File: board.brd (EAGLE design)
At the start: 26.3 x 37.5 mm, 49 parts, among them IC1 ATMEGA48/88/168-AU, IC2 TP4056, IC3 MAX31865, Q1 IRFR5305

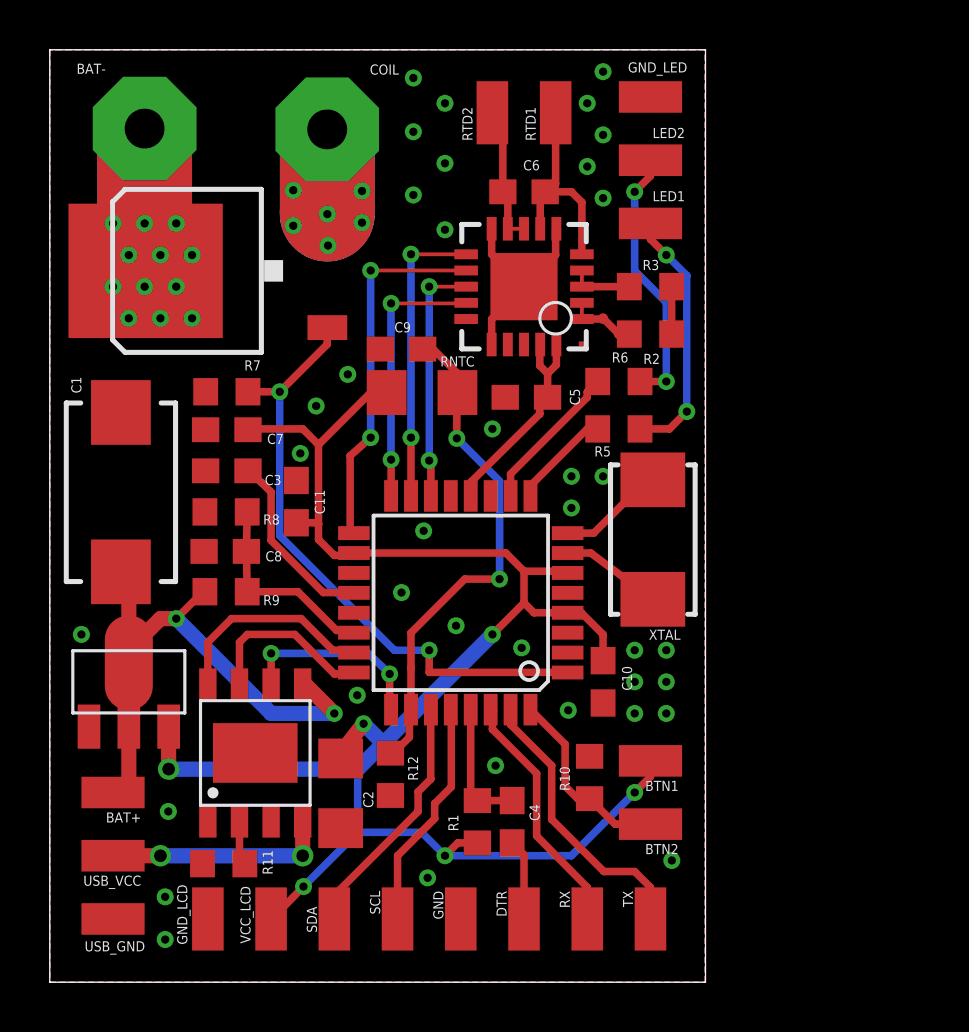
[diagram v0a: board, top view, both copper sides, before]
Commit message: cleanup of schematics
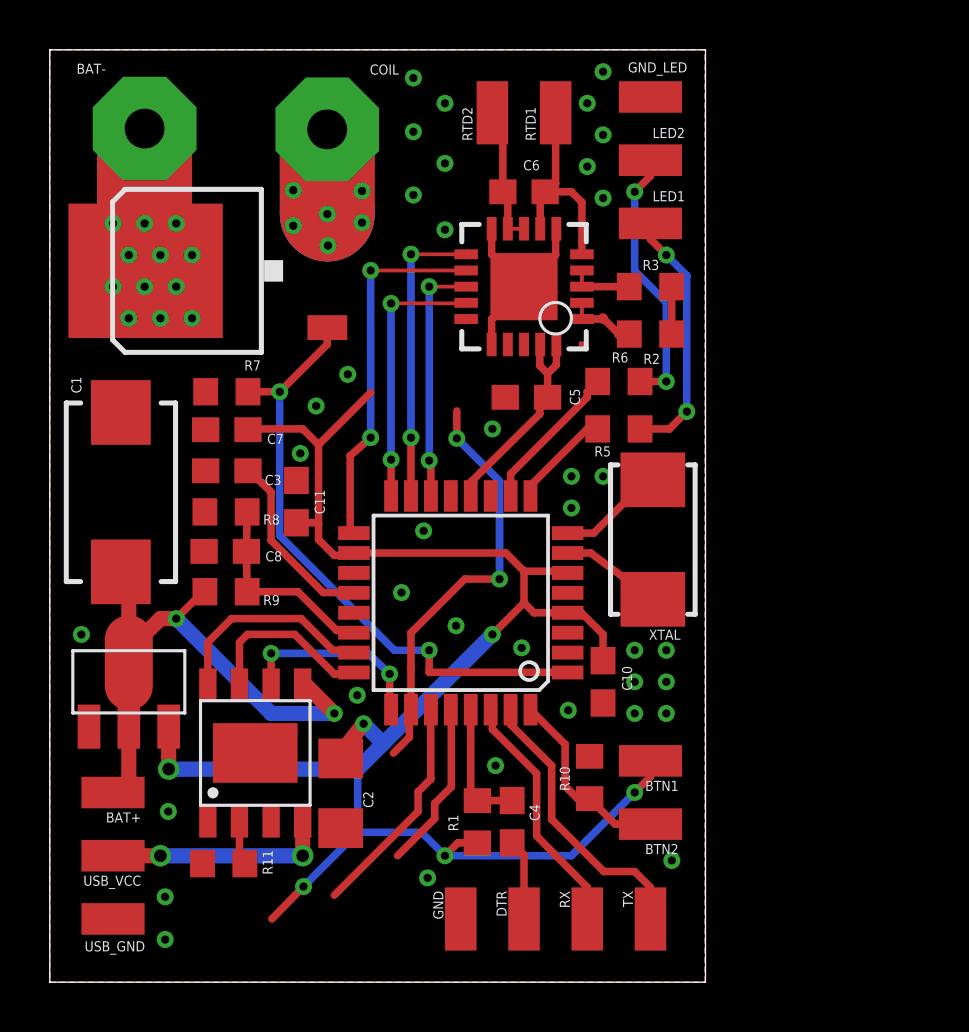
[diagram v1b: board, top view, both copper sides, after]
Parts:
- removed C9: 100n, rcl:C0603
- removed GND_LCD, SCL, SDA, VCC_LCD: (no value), wirepad:SMD1,27-2,54
- removed R12: 5.6k, rcl:R0603
- removed RNTC: (no value), resistor:R1206
- R11: value 10k -> 1,2k
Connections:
- net A3_NTC: no longer C9.2, R12.2, RNTC.2
- net A4_SDA: no longer SDA.1
- net A5_SCL: no longer SCL.1
- net GND: no longer C9.1, GND_LCD.1, R12.1
- net VCC: no longer RNTC.1, VCC_LCD.1
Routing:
- net A3_NTC: track 20.5 -> 17.0 mm
- net A5_SCL: track 9.31 -> 6.77 mm
- net A4_SDA: track 10.0 -> 9.06 mm
- net VCC: track 72.5 -> 71.9 mm

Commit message: using smaller resistors for voltage sensor
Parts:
- R8: value 10k -> 100k
- R9: value 5k -> 51k
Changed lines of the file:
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@@
 <attribute name="VALUE" x="6.477" y="21.81225" size="1.27" layer="27"/>
 </element>
-<element name="R8" library="rcl" package="R0603" value="10k" x="7.08025" y="18.89125" smashed="yes" rot="R180">
+<element name="R8" library="rcl" package="R0603" value="100k" x="7.08025" y="18.89125" smashed="yes" rot="R180">
 <attribute name="NAME" x="8.5725" y="18.38325" size="0.4064" layer="25"/>
 <attribute name="VALUE" x="7.71525" y="20.79625" size="1.27" layer="27" rot="R180"/>
 </element>
-<element name="R9" library="rcl" package="R0603" value="5k" x="7.08025" y="15.6845" smashed="yes">
+<element name="R9" library="rcl" package="R0603" value="51k" x="7.08025" y="15.6845" smashed="yes">
 <attribute name="NAME" x="8.5725" y="15.14475" size="0.4064" layer="25"/>
 <attribute name="VALUE" x="6.44525" y="13.7795" size="1.27" layer="27"/>

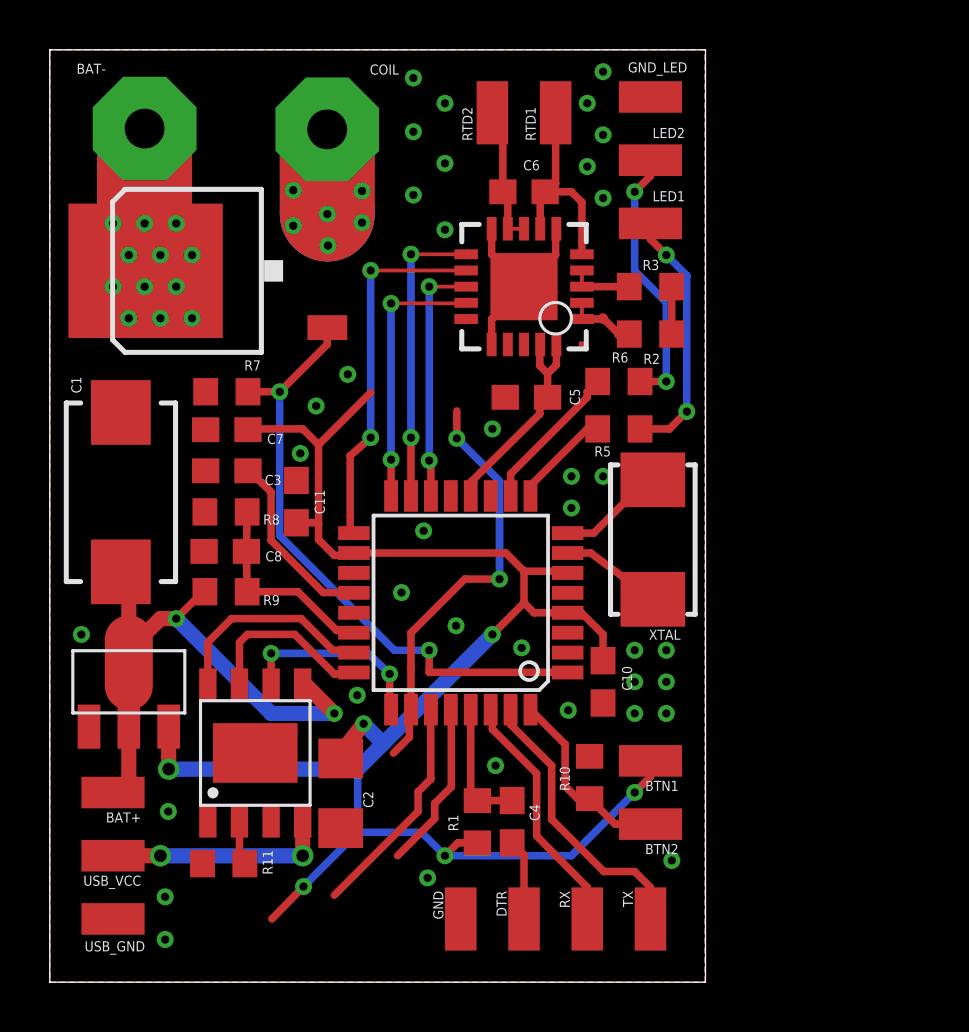
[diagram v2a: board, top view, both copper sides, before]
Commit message: using new mosfets, rearangement of parts
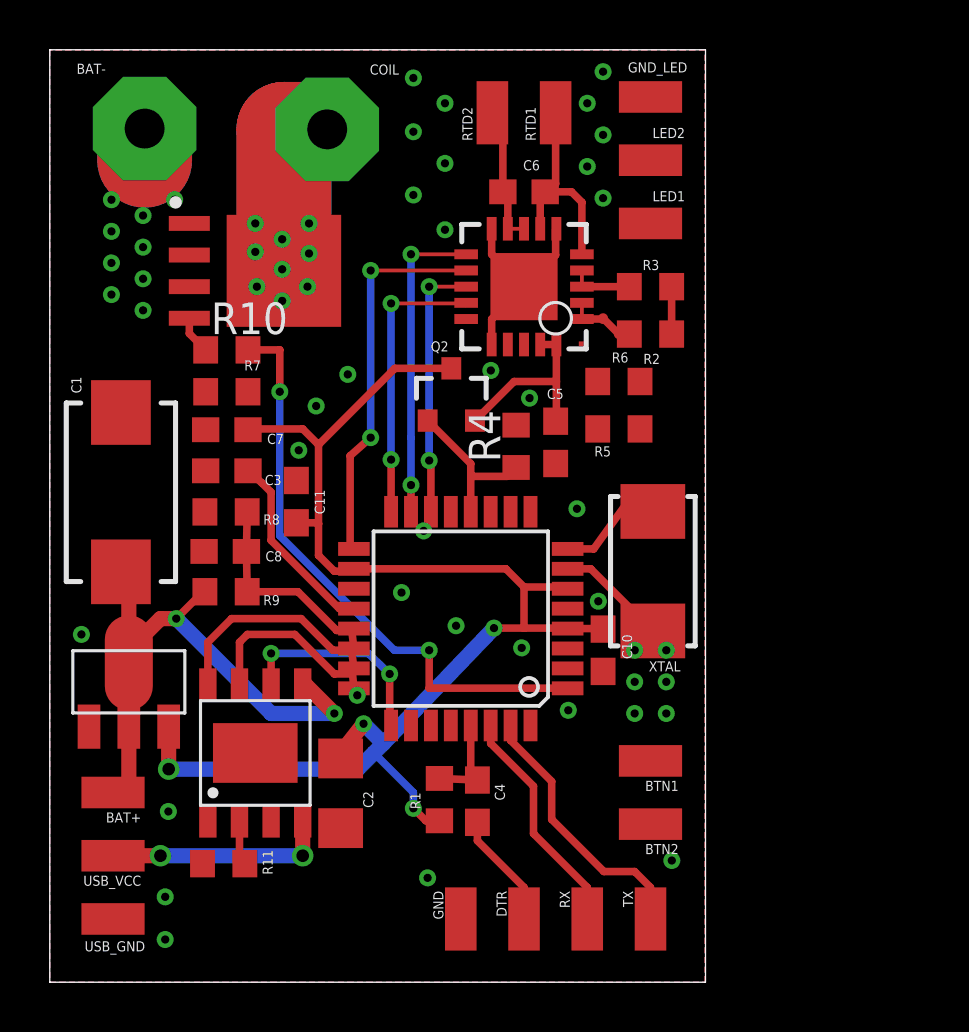
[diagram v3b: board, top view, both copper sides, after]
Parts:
- added Q2: IRLML2244, SparkFun-DiscreteSemi:SOT23-3
- added R4: 10k, rcl:R0603
- Q1: value IRFR5305 -> PH2925U; device transistor-power:D-PAK_TO252AA -> selfmade:SOT-669
- R10: value 10k -> 100
- moved R10 22.5 mm to (7.11, 25.4), turned to 0 degrees
- moved Q1 3.18 mm to (9.53, 28.6), turned to 0 degrees
- moved C5 2.16 mm to (20.3, 21.7), turned to 270 degrees
- moved R1 1.76 mm to (15.7, 7.33)
- moved C4 1.62 mm to (17.2, 7.27)
- moved C10 1.27 mm to (22.2, 13.3)
- moved XTAL 1.27 mm to (24.2, 16.5)
- moved IC1 0.63 mm to (16.5, 14.6)
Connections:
- net A3_NTC renamed A3
- net A4_SDA renamed A4
- net A5_SCL renamed A5
- new net GATE: Q1.4, R10.1, R7.2
- new net VCC_MAX: C5.1, IC3.19, IC3.20, Q2.2
- net COIL: now also Q1.5; no longer Q1.3
- net D2_BUTTON: now also BTN1.1; no longer BTN2.1, R10.1
- net D3_GATE: now also R10.2; no longer Q1.1, R7.2
- net D8_VCC_MAX: now also Q2.1, R4.1; no longer C5.1, IC3.19, IC3.20
- net GND: now also Q1.1, Q1.2, Q1.3, R4.2; no longer Q1.4, R10.2
- net VCC: now also Q2.3; no longer BTN1.1
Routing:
- net A3: track 17.0 -> 0.00 mm, vias 2 -> 0
- net VCC: track 71.9 -> 56.0 mm, vias 6 -> 4
- net LED2: track 10.7 -> 0.00 mm, vias 2 -> 0
- net LED1: track 10.3 -> 0.00 mm, vias 2 -> 0
- net A4: track 9.06 -> 0.00 mm
- net COIL: track 6.82 -> 14.8 mm, vias 6 -> 0
- net D2_BUTTON: track 7.71 -> 0.00 mm
- net VCC_MAX: track 0.00 -> 7.66 mm
- net GND: track 18.2 -> 10.6 mm, vias 49 -> 45
- net A5: track 6.77 -> 0.00 mm
- net D6_LED2: track 6.05 -> 0.00 mm
- net D5_LED1: track 4.06 -> 0.00 mm
- net D8_VCC_MAX: track 8.82 -> 6.35 mm
- net GATE: track 0.00 -> 1.54 mm
- net RST: track 5.32 -> 3.83 mm
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
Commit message: adding 3rd LED, new regulator, shrinking board
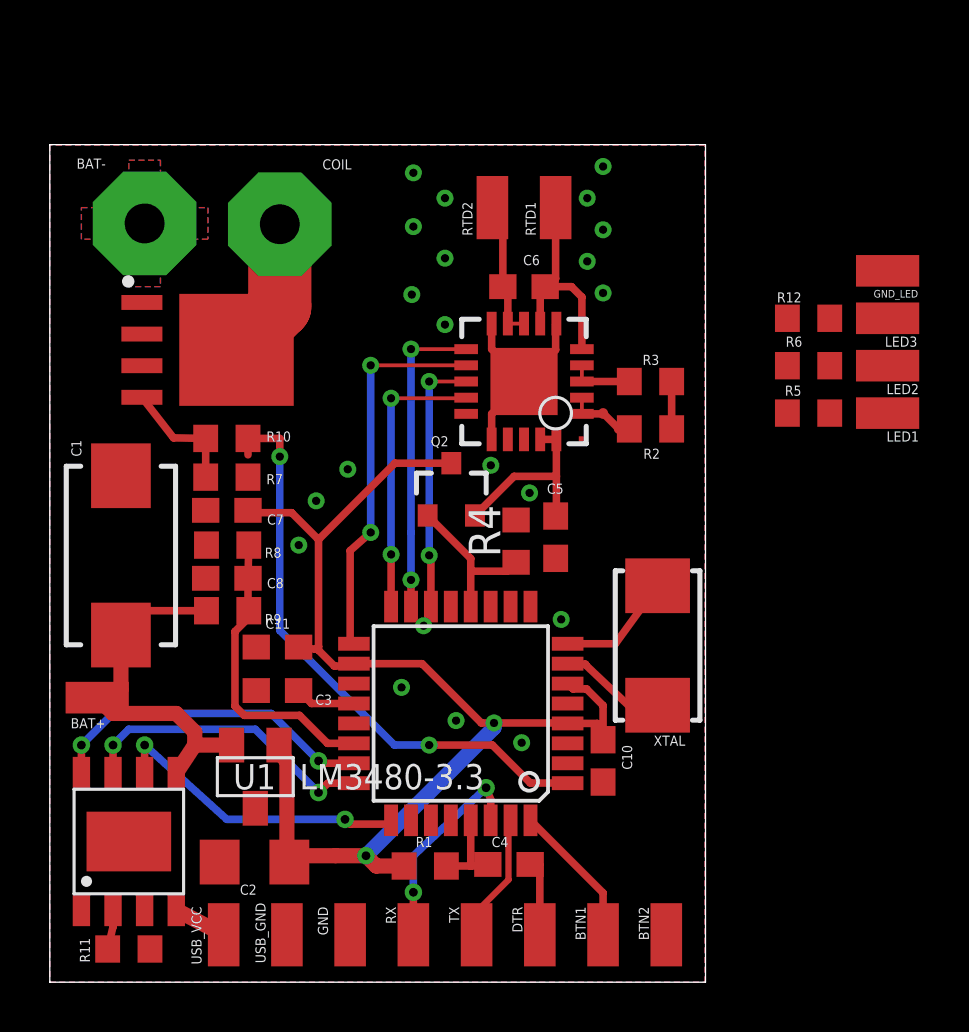
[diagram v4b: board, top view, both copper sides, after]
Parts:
- removed U$2: TS9011, selfmade:SOT89
- added LED3: (no value), wirepad:SMD1,27-2,54
- added R12: 1K, rcl:R0603
- added U1: LM3480-3.3, regulators:SOT-23-3
- moved LED2 12.6 mm to (33.7, 24.8)
- moved LED1 12.2 mm to (33.7, 22.9)
- moved GND_LED 11.8 mm to (33.7, 28.6)
- moved C3 9.06 mm to (9.14, 11.7)
- moved R5 7.65 mm to (30.5, 22.9)
- moved R6 7.65 mm to (30.5, 24.8)
- moved BTN1 7.24 mm to (22.2, 1.91), turned to 180 degrees
- moved USB_GND 7.01 mm to (9.53, 1.91), turned to 180 degrees
- moved RX 7.01 mm to (14.6, 1.91)
- moved TX 7.01 mm to (17.1, 1.91)
- moved IC2 6.20 mm to (3.17, 5.65)
- moved C11 5.89 mm to (9.14, 13.5), turned to 0 degrees
- moved USB_VCC 5.46 mm to (6.99, 1.91), turned to 180 degrees
- moved R11 5.13 mm to (3.17, 1.33), turned to 0 degrees
- moved GND 4.49 mm to (12.1, 1.91)
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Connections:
- removed net D9: IC1.13
- new net D9_LED3: IC1.13, R12.2
- new net LED3: LED3.1, R12.1
- net GND: now also BTN2.1, U1.3; no longer U$2.GND
- net VBAT: now also U1.2; no longer U$2.IN1, U$2.IN2
- net VCC: now also U1.1; no longer U$2.OUT
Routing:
- net COIL: track 14.8 -> 5.22 mm
- net VCC: track 56.0 -> 48.7 mm, vias 4 -> 2
- net VUSB: track 9.00 -> 2.15 mm, vias 2 -> 0
- net VBAT: track 20.9 -> 14.9 mm, vias 2 -> 0
- net D2_BUTTON: track 0.00 -> 5.80 mm
- net TXO: track 10.8 -> 5.16 mm
- net AREF: track 7.66 -> 2.44 mm
- net A1_CHRG_STAT: track 7.60 -> 12.3 mm, vias 0 -> 2
- net A0_CHRG_EN: track 9.12 -> 13.4 mm, vias 0 -> 2
- net A2_CHRG_STBY: track 8.42 -> 12.3 mm
- net GATE: track 1.54 -> 4.91 mm
- net A7_VSENS: track 8.78 -> 12.1 mm
- net GND: track 10.6 -> 8.06 mm, vias 45 -> 21
- net DTR: track 4.66 -> 3.21 mm
- net RXI: track 9.38 -> 8.72 mm, vias 0 -> 2
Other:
- board size 26.3 x 37.5 mm -> 26.3 x 33.6 mm
- board text added: "Vapoduino_v0.2"
- board text removed: "Vapoduino_v0.1"

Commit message: first draft of new layout
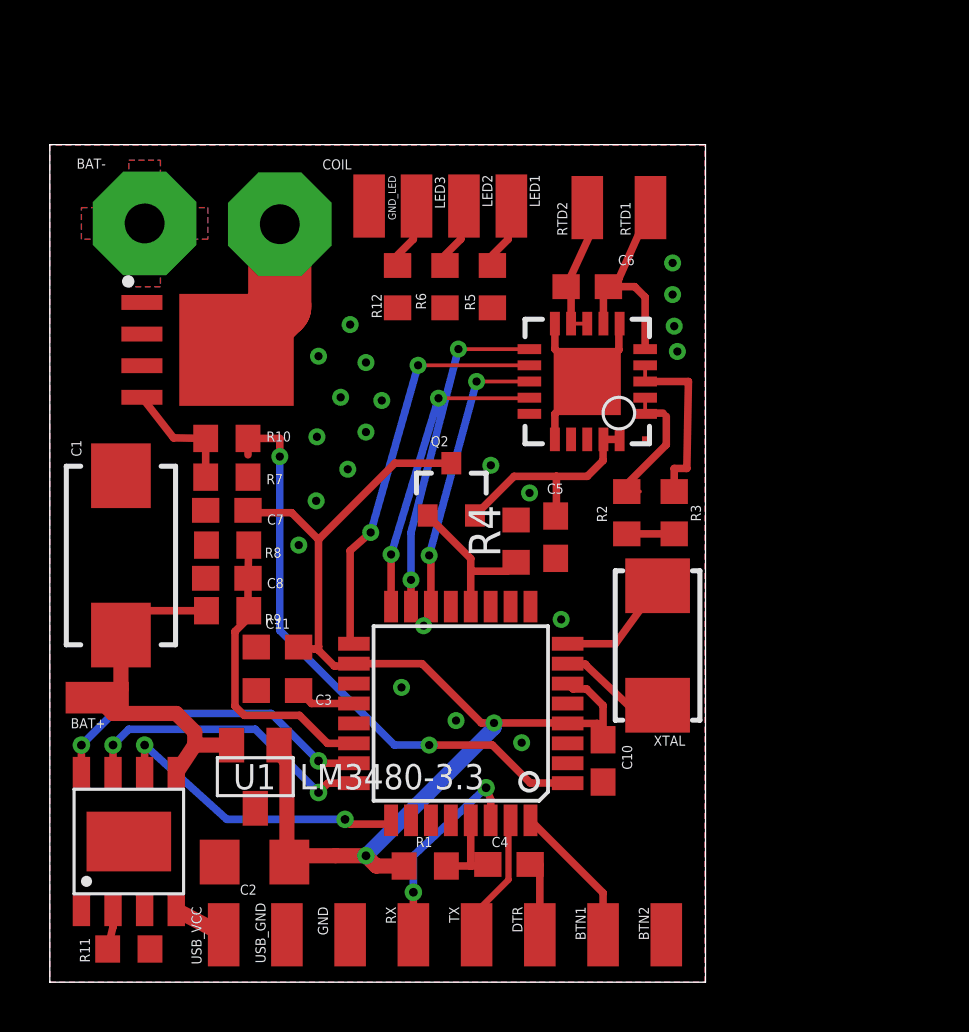
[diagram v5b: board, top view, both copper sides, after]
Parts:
- moved GND_LED 21.0 mm to (12.8, 31.2), turned to 180 degrees
- moved LED3 19.5 mm to (14.7, 31.2), turned to 0 degrees
- moved LED2 18.2 mm to (16.6, 31.2), turned to 180 degrees
- moved LED1 17.3 mm to (18.5, 31.2), turned to 180 degrees
- moved R12 16.6 mm to (14.0, 27.9), turned to 270 degrees
- moved R6 14.9 mm to (15.9, 27.9), turned to 270 degrees
- moved R5 13.7 mm to (17.8, 27.9), turned to 270 degrees
- moved R3 5.36 mm to (25.1, 18.9), turned to 270 degrees
- moved RTD1 3.81 mm to (24.1, 31.1)
- moved RTD2 3.81 mm to (21.6, 31.1)
- moved R2 3.50 mm to (23.2, 18.9), turned to 90 degrees
- moved C6 2.54 mm to (21.6, 27.9)
- moved IC3 2.54 mm to (21.6, 24.1)
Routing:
- net TEMP_REF-: track 2.56 -> 7.32 mm
- net TEMP_REF+: track 2.85 -> 5.78 mm
- net LED2: track 0.00 -> 2.70 mm
- net LED1: track 0.00 -> 2.70 mm
- net LED3: track 0.00 -> 2.70 mm
- net VCC_MAX: track 7.66 -> 9.19 mm
- net D12_MISO: track 11.4 -> 12.3 mm
- net D13_SCK: track 15.5 -> 16.4 mm
- net D10_CS: track 10.6 -> 11.4 mm
- net D11_MOSI: track 12.6 -> 13.4 mm

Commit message: adding vias for mosfet
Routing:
- net COIL: track 5.22 -> 11.0 mm, vias 0 -> 9
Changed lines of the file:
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@@
 <layer number="14" name="Route14" color="1" fill="6" visible="yes" active="yes"/>
 <layer number="15" name="Route15" color="4" fill="6" visible="yes" active="yes"/>
-<layer number="16" name="Bottom" color="1" fill="1" visible="no" active="yes"/>
+<layer number="16" name="Bottom" color="1" fill="1" visible="yes" active="yes"/>
 <layer number="17" name="Pads" color="2" fill="1" visible="yes" active="yes"/>
 <layer number="18" name="Vias" color="2" fill="1" visible="yes" active="yes"/>
@@
 <wire x1="0" y1="33.645" x2="0" y2="0" width="0" layer="20"/>
 <text x="25.4" y="0.635" size="1.6764" layer="22" rot="MR0">Vapoduino_v0.2</text>
+<rectangle x1="5.207" y1="23.114" x2="9.779" y2="27.686" layer="16"/>
 </plain>
 <attributes>
@@
 <contactref element="COIL" pad="1"/>
 <contactref element="Q1" pad="5"/>
-<wire x1="9.23925" y1="30.44825" x2="9.23925" y2="27.13925" width="2.54" layer="1"/>
-<wire x1="9.23925" y1="27.13925" x2="7.88750625" y2="25.78750625" width="2.54" layer="1"/>
-<wire x1="7.5" y1="25.4" x2="7.88750625" y2="25.78750625" width="0" layer="19" extent="1-1"/>
+<wire x1="9.23925" y1="30.44825" x2="9.23925" y2="27.01225" width="3.81" layer="1"/>
+<wire x1="9.23925" y1="27.01225" x2="7.88750625" y2="25.78750625" width="2.54" layer="1"/>
+<wire x1="9.23925" y1="30.44825" x2="9.23925" y2="27.01925" width="3.81" layer="16"/>
+<wire x1="9.23925" y1="27.01925" x2="7.62" y2="25.4" width="2.54" layer="16"/>
+<via x="5.9055" y="27.1145" extent="1-16" drill="0.35"/>
+<via x="7.8105" y="27.1145" extent="1-16" drill="0.35"/>
+<via x="9.7155" y="27.1145" extent="1-16" drill="0.35"/>
+<via x="6.858" y="25.9715" extent="1-16" drill="0.35"/>
+<via x="8.763" y="25.9715" extent="1-16" drill="0.35"/>
+<via x="7.8105" y="24.5745" extent="1-16" drill="0.35"/>
+<via x="5.9055" y="24.5745" extent="1-16" drill="0.35"/>
+<via x="6.858" y="23.5585" extent="1-16" drill="0.35"/>
+<via x="8.763" y="23.5585" extent="1-16" drill="0.35"/>
+<wire x1="7.5" y1="25.4" x2="7.62" y2="25.4" width="0" layer="19" extent="1-16"/>
+<wire x1="9.7155" y1="27.1145" x2="9.23925" y2="27.01925" width="0" layer="19" extent="16-16"/>
+<wire x1="6.858" y1="25.9715" x2="7.5" y2="25.4" width="0" layer="19" extent="1-1"/>
+<wire x1="7.8105" y1="24.5745" x2="7.62" y2="25.4" width="0" layer="19" extent="16-16"/>
+<wire x1="8.763" y1="25.9715" x2="7.88750625" y2="25.78750625" width="0" layer="19" extent="1-1"/>
+<wire x1="7.8105" y1="27.1145" x2="7.88750625" y2="25.78750625" width="0" layer="19" extent="1-1"/>
+<wire x1="8.763" y1="23.5585" x2="7.8105" y2="24.5745" width="0" layer="19" extent="1-1"/>
+<wire x1="6.858" y1="23.5585" x2="7.8105" y2="24.5745" width="0" layer="19" extent="1-1"/>
+<wire x1="5.9055" y1="24.5745" x2="6.858" y2="23.5585" width="0" layer="19" extent="1-1"/>
+<wire x1="5.9055" y1="27.1145" x2="6.858" y2="25.9715" width="0" layer="19" extent="1-1"/>
 </signal>
 <signal name="N$1">

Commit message: connect leds via bottom
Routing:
- net D6_LED2: track 0.00 -> 13.8 mm, vias 0 -> 2
- net D5_LED1: track 0.00 -> 13.1 mm, vias 0 -> 2
- net D9_LED3: track 0.00 -> 11.9 mm, vias 0 -> 2
- net D11_MOSI: track 13.4 -> 17.8 mm
- net D13_SCK: track 16.4 -> 20.7 mm
- net D10_CS: track 11.4 -> 15.8 mm
- net D12_MISO: track 12.3 -> 16.6 mm
- net TEMP_REF+: track 5.78 -> 7.40 mm
- net TEMP_REF-: track 7.32 -> 8.21 mm
- net GND: vias 21 -> 14
